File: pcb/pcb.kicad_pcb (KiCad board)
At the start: 2 copper layers, 33 parts, among them J1 USB_C_Receptacle_USB2.0_14P, J2 Conn_01x20, J3 Conn_01x20, J4 Conn_01x03, SW1 SW_Push, U1 RP2040, U2 NCP1117-3.3_SOT223, U3 W25Q128JVS, Y1 12 MHz

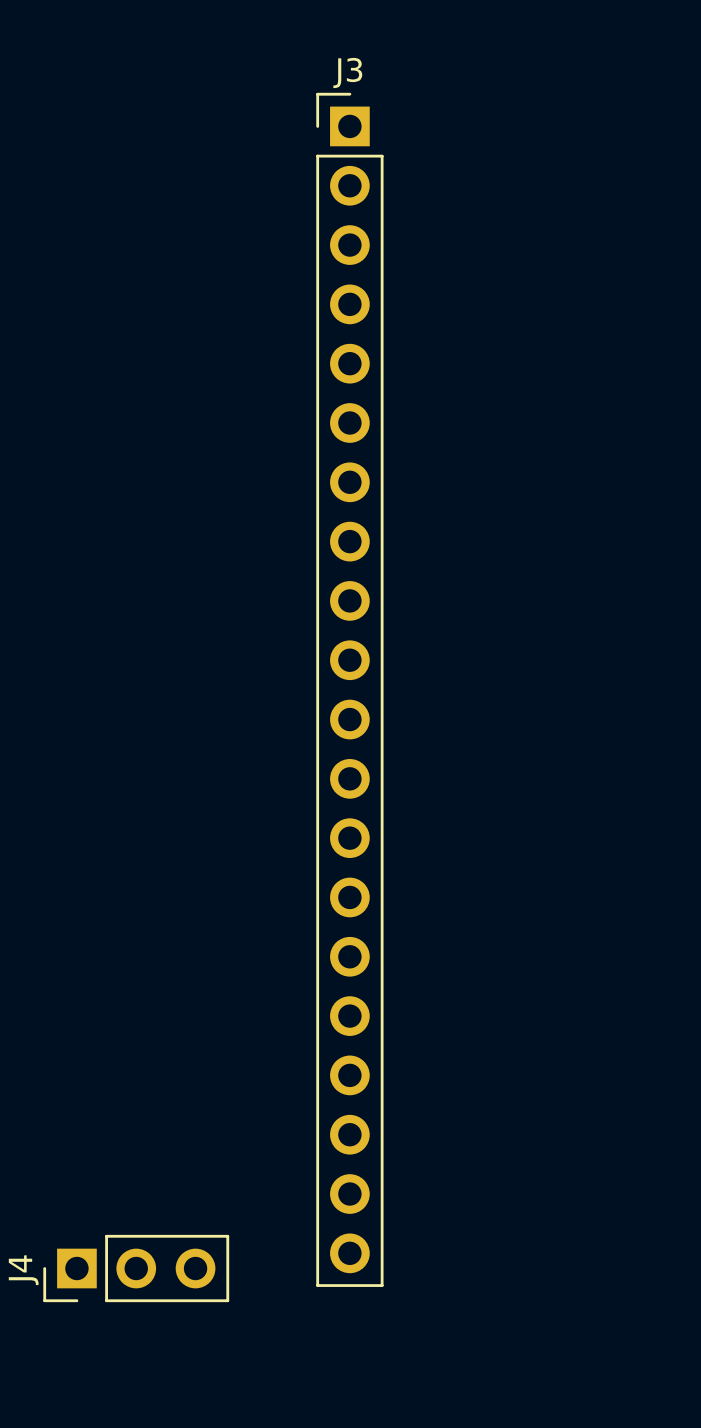
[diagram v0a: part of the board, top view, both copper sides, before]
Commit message: feat: added the neopixel status led
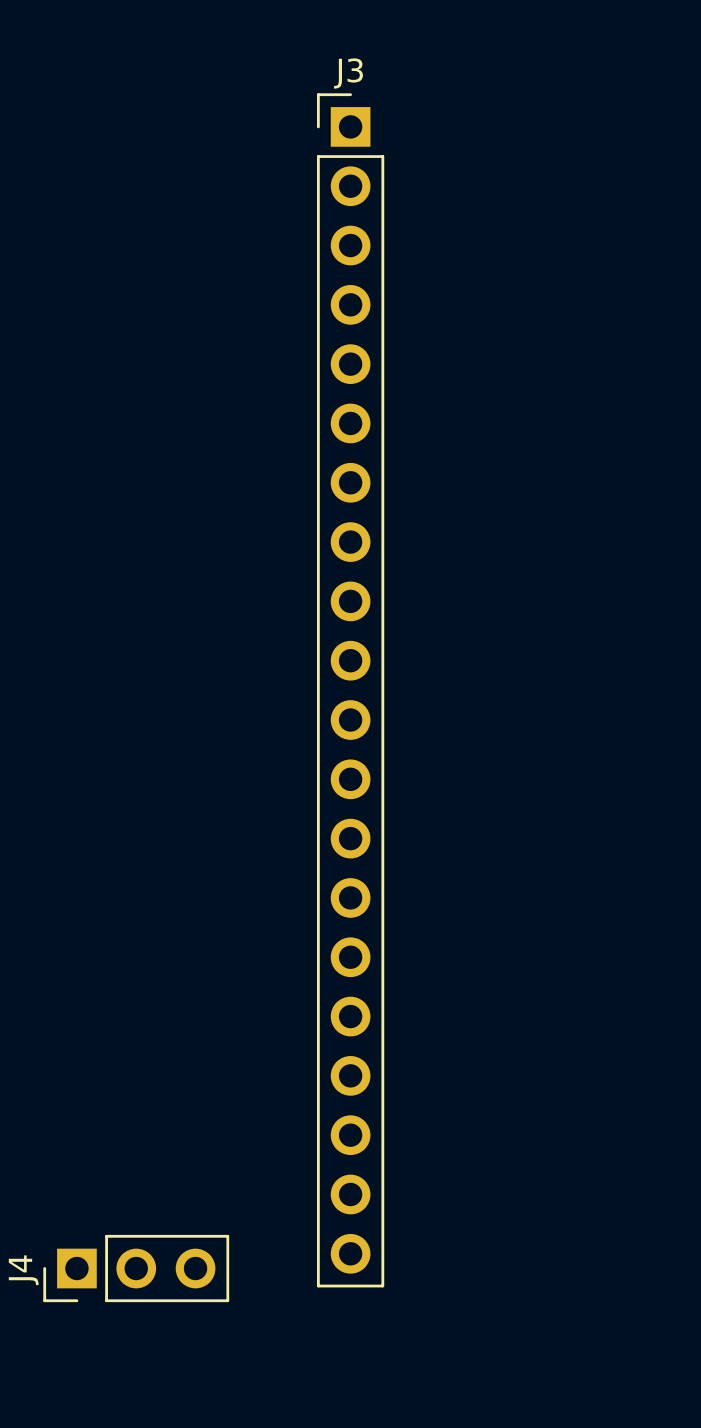
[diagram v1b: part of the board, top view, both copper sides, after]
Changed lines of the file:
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@@
 	(footprint "Connector_PinHeader_2.54mm:PinHeader_1x20_P2.54mm_Vertical"
 		(layer "F.Cu")
-		(at 133.35 61.94)
+		(at 133.38 61.96)
 		(descr "Through hole straight pin header, 1x20, 2.54mm pitch, single row")
 		(tags "Through hole pin header THT 1x20 2.54mm single row")
@@
 			)
 		)
+	)
+	(dimension
+		(type orthogonal)
+		(layer "F.Cu")
+		(pts
+			(xy 135.15 111.99) (xy 114.15 111.99)
+		)
+		(height 3.35)
+		(orientation 0)
+		(format
+			(prefix "")
+			(suffix "")
+			(units 3)
+			(units_format 0)
+			(precision 4)
+			(suppress_zeroes yes)
+		)
+		(style
+			(thickness 0.2)
+			(arrow_length 1.27)
+			(text_position_mode 0)
+			(arrow_direction outward)
+			(extension_height 0.58642)
+			(extension_offset 0.5)
+			(keep_text_aligned yes)
+		)
+		(gr_text "21"
+			(at 124.65 113.54 0)
+			(layer "F.Cu")
+			(effects
+				(font
+					(size 1.5 1.5)
+					(thickness 0.3)
+				)
+			)
+		)

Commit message: finished the schematic and added it to the pcb
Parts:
- added D2: APA102, LED_SMD:LED_RGB_5050-6, F.Cu at (201.1, 61.7)
- moved J1 18.5 mm to (184.9, 92.1)
- moved U1 15.4 mm to (186.9, 104.5)
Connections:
- J2 pad 11: GPIO8 -> unconnected-(J2-Pin_11-Pad11)
- J2 pad 12: GPIO9 -> unconnected-(J2-Pin_12-Pad12)

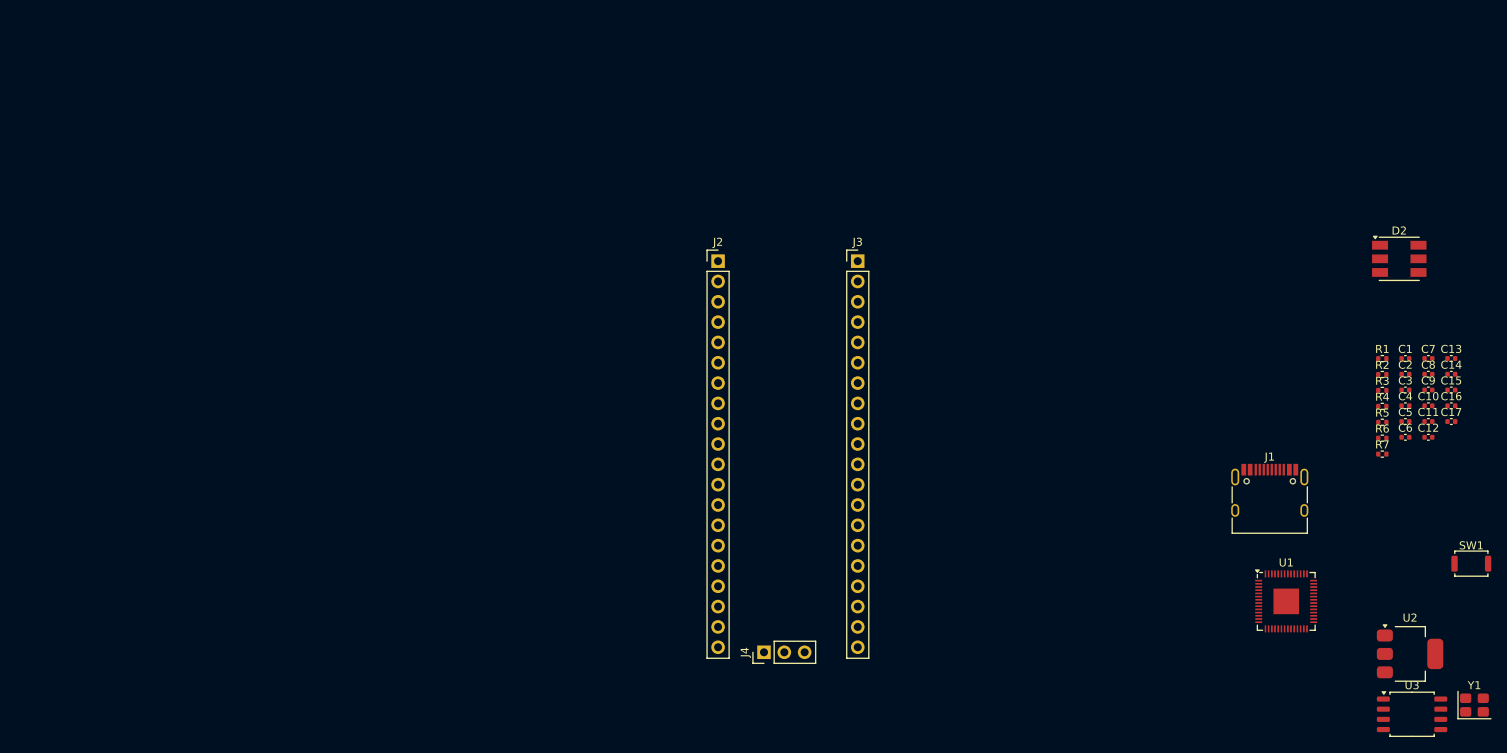
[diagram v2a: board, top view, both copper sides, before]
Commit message: updated the schematic with better formatting
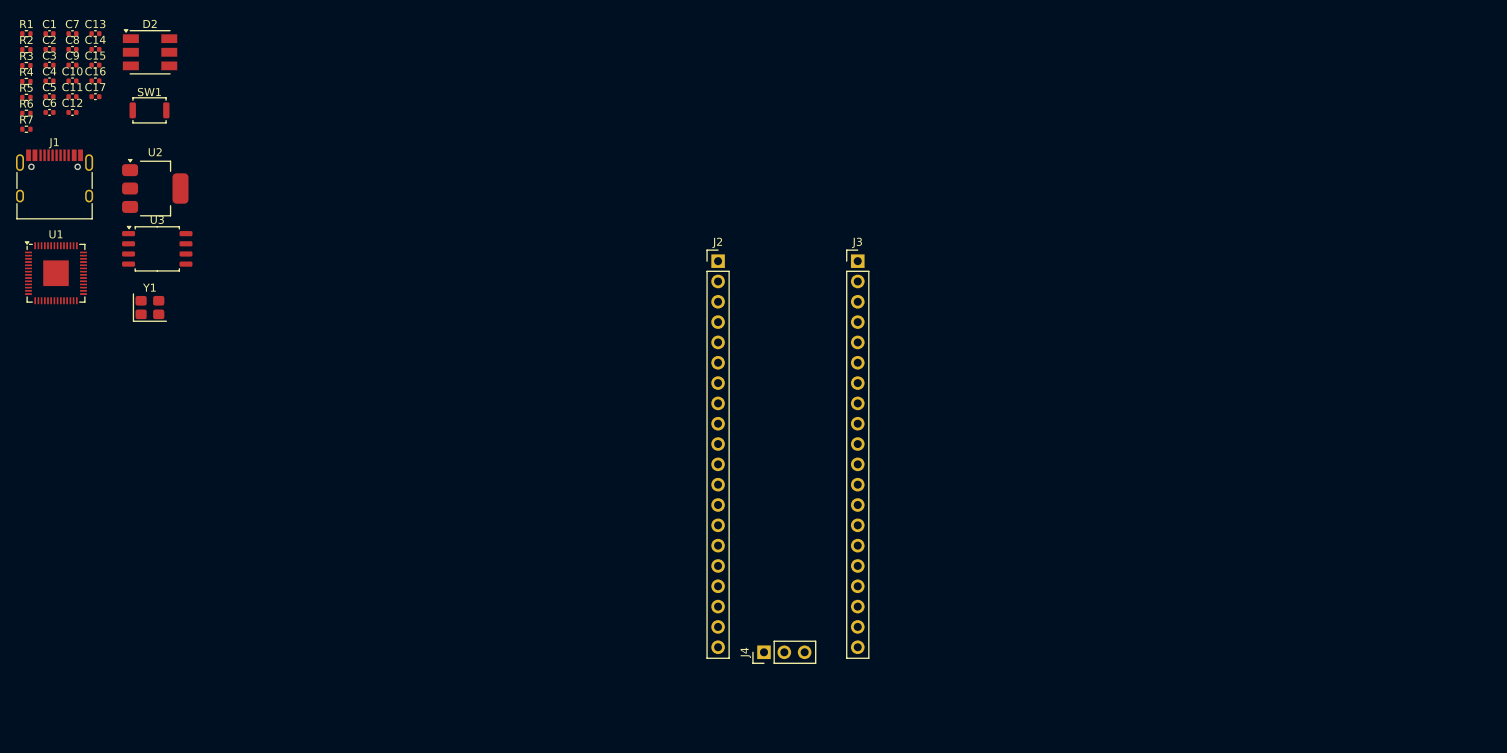
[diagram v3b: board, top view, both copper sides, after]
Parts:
- moved SW1 174.7 mm to (44.9, 43.1)
- moved C1 174.3 mm to (32.4, 33.5)
- moved C10 174.3 mm to (35.2, 39.4)
- moved C11 174.3 mm to (35.2, 41.4)
- moved C12 174.3 mm to (35.2, 43.4)
- moved C13 174.3 mm to (38.1, 33.5)
- moved C14 174.3 mm to (38.1, 35.5)
- moved C15 174.3 mm to (38.1, 37.5)
- moved C16 174.3 mm to (38.1, 39.4)
- moved C17 174.3 mm to (38.1, 41.4)
- moved C2 174.3 mm to (32.4, 35.5)
- moved C3 174.3 mm to (32.4, 37.5)
- moved C4 174.3 mm to (32.4, 39.4)
- moved C5 174.3 mm to (32.4, 41.4)
- moved C6 174.3 mm to (32.4, 43.4)
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
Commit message: feat: updated most of the pcb, still have some capacitors to wire
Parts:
- added C18: 0.1uF, Capacitor_SMD:C_0402_1005Metric, F.Cu at (131.5, 99.3)
- added R8: 100, Resistor_SMD:R_0402_1005Metric, F.Cu at (132.0, 94.5)
- added R9: 100, Resistor_SMD:R_0402_1005Metric, F.Cu at (132.0, 96.5)
- C1: value 0.1uF -> 1uF
- C9: value 1uF -> 0.1uF
- U2: value NCP1117-3.3_SOT223 -> MCP1700x-330xxTT; footprint Package_TO_SOT_SMD:SOT-223-3_TabPin2 -> Package_TO_SOT_SMD:SOT-23
- U3: value W25Q128JVS -> W25Q16JVZPIQ; footprint Package_SO:SOIC-8_5.3x5.3mm_P1.27mm -> Package_SON:Winbond_USON-8-1EP_3x2mm_P0.5mm_EP0.2x1.6mm
- moved C10 97.1 mm to (113.5, 96.8), turned to 90 degrees
- moved C7 96.3 mm to (120.8, 77.6), turned to 90 degrees
- moved C2 94.6 mm to (103.3, 98.0), turned to -90 degrees
- moved C6 94.2 mm to (119.8, 78.2), turned to -90 degrees
- moved C1 91.8 mm to (106.8, 87.2), turned to 45 degrees
- moved R5 91.6 mm to (101.7, 97.8)
- moved C9 90.7 mm to (106.9, 93.1)
- moved D2 90.3 mm to (101.4, 106.3)
- moved C8 89.1 mm to (106.7, 88.7)
- moved C16 89.0 mm to (103.3, 100.0), turned to 90 degrees
- moved R3 87.9 mm to (102.2, 86.8), turned to -90 degrees
- moved R4 87.7 mm to (103.3, 86.8), turned to -90 degrees
- moved C15 86.7 mm to (97.9, 100.2), turned to -90 degrees
- moved C5 86.2 mm to (105.3, 87.3), turned to 90 degrees
- moved C3 85.0 mm to (96.3, 93.4), turned to 180 degrees
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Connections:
- C17 pad 1: +3V3 -> GND
- C17 pad 2: GND -> +3V3
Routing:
- net +3V3: track 0.00 -> 67.8 mm, vias 0 -> 3
- net GPIO0: track 0.00 -> 26.8 mm, vias 0 -> 1
- net GPIO1: track 0.00 -> 25.0 mm, vias 0 -> 2
- net GPIO15: track 0.00 -> 23.5 mm
- net GPIO29_ADC3: track 0.00 -> 23.4 mm, vias 0 -> 1
- net SWCLK: track 0.00 -> 22.8 mm, vias 0 -> 1
- net GPIO16: track 0.00 -> 21.7 mm
- net SWD: track 0.00 -> 21.7 mm, vias 0 -> 1
- net GPIO14: track 0.00 -> 20.8 mm
- net GPIO2: track 0.00 -> 20.4 mm, vias 0 -> 2
- net GPIO28_ADC2: track 0.00 -> 20.1 mm
- net VBUS: track 0.00 -> 20.0 mm
- net USB_D-: track 0.00 -> 19.9 mm
- net GPIO17: track 0.00 -> 19.4 mm
- net QSPI_SS: track 0.00 -> 19.1 mm, vias 0 -> 2
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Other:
- board outline added: 21 x 51 mm

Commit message: holy shit massive update the pcb routing is done
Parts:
- moved R8 37.2 mm to (96.7, 106.3)
- moved R9 36.3 mm to (96.6, 104.8)
- moved C18 27.1 mm to (105.7, 107.6), turned to 90 degrees
- moved C7 19.3 mm to (102.3, 83.0), turned to 180 degrees
- moved C6 18.2 mm to (102.8, 84.4), turned to 90 degrees
- moved C10 9.01 mm to (104.5, 98.1), turned to -90 degrees
- moved J2 0.09 mm to (92.5, 66.2)
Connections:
- J2 pad 11: unconnected-(J2-Pin_11-Pad11) -> GPIO8
- J2 pad 12: unconnected-(J2-Pin_12-Pad12) -> GPIO9
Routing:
- net GND: track 9.28 -> 112.6 mm, vias 4 -> 41
- net +3V3: track 67.8 -> 99.7 mm, vias 3 -> 6
- net GPIO8: track 0.00 -> 26.6 mm, vias 0 -> 2
- net +1V1: track 5.54 -> 28.6 mm, vias 0 -> 2
- net GPIO9: track 0.00 -> 20.5 mm, vias 0 -> 2
- net XIN: track 1.71 -> 12.2 mm, vias 0 -> 2
- net XOUT: track 0.00 -> 2.58 mm
- net Net-(D2-DI): track 0.00 -> 1.96 mm
- net Net-(D2-CI): track 0.00 -> 1.84 mm
- net GPIO29_ADC3: track 23.4 -> 25.1 mm
- net USB_D+: track 18.6 -> 20.3 mm
- net USB_D-: track 19.9 -> 20.8 mm
- net GPIO1: track 25.0 -> 24.9 mm, vias 2 -> 1
- added copper zone on B.Cu, net GND
- added copper zone on F.Cu, net GND
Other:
- board size 21 x 51 mm -> 21 x 51.1 mm

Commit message: better routing completed
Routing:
- net GND: track 112.6 -> 112.8 mm, vias 41 -> 82

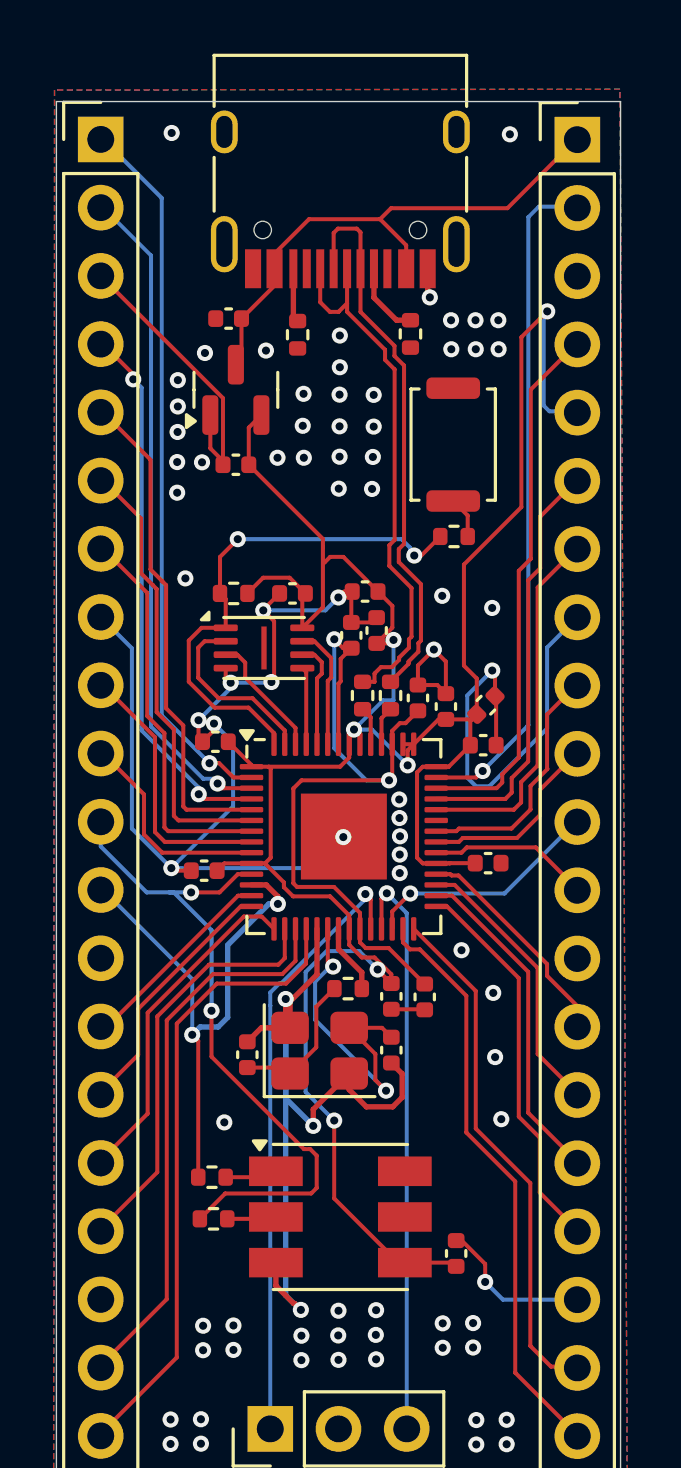
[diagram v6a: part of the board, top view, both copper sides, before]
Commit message: added some more vias and lined them up
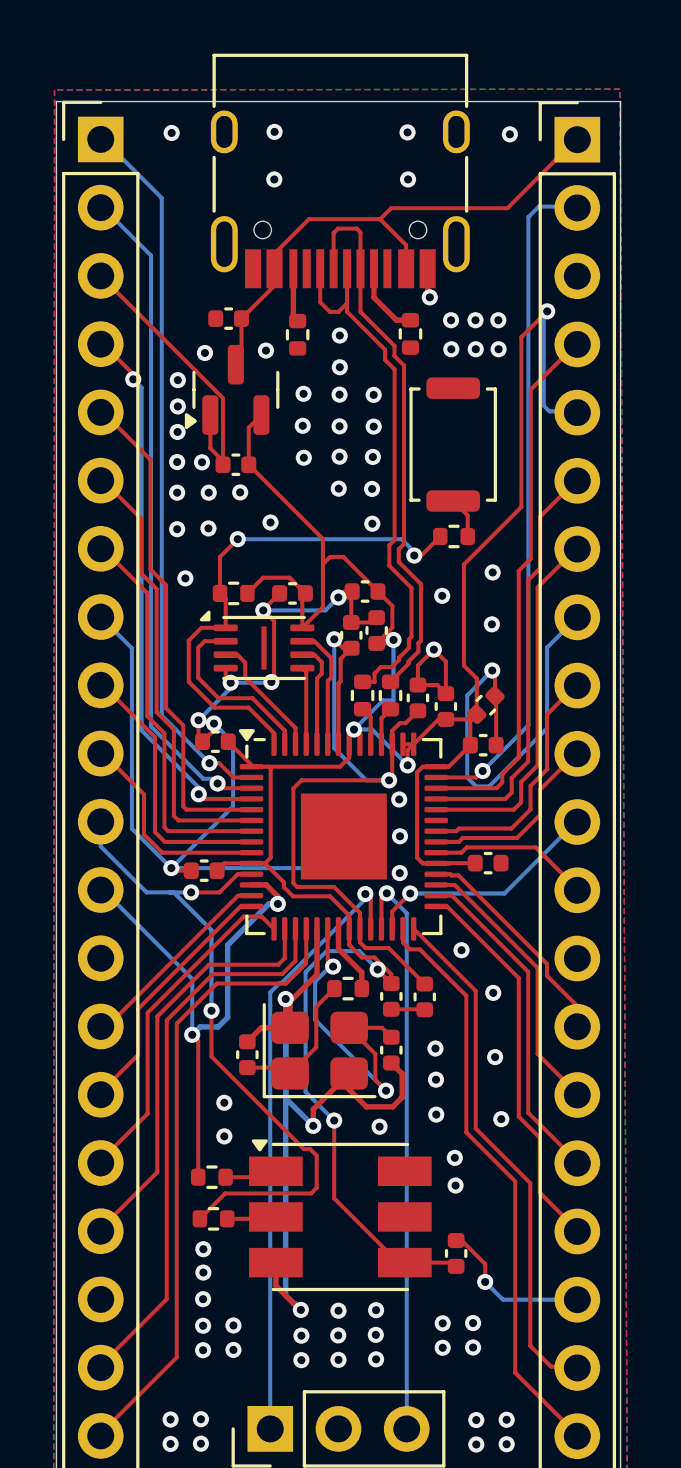
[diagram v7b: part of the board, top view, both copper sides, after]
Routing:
- net GND: vias 82 -> 99
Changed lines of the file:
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@@
 	)
 	(via
-		(at 103.61 92.77)
-		(size 0.6)
-		(drill 0.3)
-		(layers "F.Cu" "B.Cu")
-		(net 1)
-	)
-	(via
 		(at 105.19 83.14)
 		(size 0.6)
@@
 	)
 	(via
-		(at 101.51 92.12)
+		(at 95.108172 93.274999)
 		(size 0.6)
 		(drill 0.3)
@@
 	)
 	(via
-		(at 95.108172 93.274999)
+		(at 107.28 72.88)
 		(size 0.6)
 		(drill 0.3)
 		(layers "F.Cu" "B.Cu")
+		(free yes)
 		(net 1)
 	)
 	(via
-		(at 107.28 72.88)
+		(at 98.8 80.41)
 		(size 0.6)
 		(drill 0.3)
@@
 	)
 	(via
+		(at 96.29 109.32)
+		(size 0.6)
+		(drill 0.3)
+		(layers "F.Cu" "B.Cu")
+		(free yes)
+		(net 1)
+	)
+	(via
 		(at 96.12 87.77)
 		(size 0.6)
@@
 	)
 	(via
+		(at 98.94 67.64)
+		(size 0.6)
+		(drill 0.3)
+		(layers "F.Cu" "B.Cu")
+		(free yes)
+		(net 1)
+	)
+	(via
 		(at 99.95 110.68)
 		(size 0.6)
@@
 	)
 	(via
+		(at 102.86 102.9)
+		(size 0.6)
+		(drill 0.3)
+		(layers "F.Cu" "B.Cu")
+		(free yes)
+		(net 1)
+	)
+	(via
+		(at 104.94 99.99)
+		(size 0.6)
+		(drill 0.3)
+		(layers "F.Cu" "B.Cu")
+		(free yes)
+		(net 1)
+	)
+	(via
 		(at 96.29 110.31)
 		(size 0.6)
@@
 	)
 	(via
+		(at 102.59 80.455)
+		(size 0.6)
+		(drill 0.3)
+		(layers "F.Cu" "B.Cu")
+		(free yes)
+		(net 1)
+	)
+	(via
 		(at 99.365 98.14726)
 		(size 0.6)
@@
 	)
 	(via
+		(at 103.92 67.64)
+		(size 0.6)
+		(drill 0.3)
+		(layers "F.Cu" "B.Cu")
+		(free yes)
+		(net 1)
+	)
+	(via
+		(at 97.67 79.29)
+		(size 0.6)
+		(drill 0.3)
+		(layers "F.Cu" "B.Cu")
+		(free yes)
+		(net 1)
+	)
+	(via
 		(at 98.53079 83.680908)
 		(size 0.6)
@@
 	)
 	(via
+		(at 104.97 102.45)
+		(size 0.6)
+		(drill 0.3)
+		(layers "F.Cu" "B.Cu")
+		(free yes)
+		(net 1)
+	)
+	(via
 		(at 106.34 110.21)
 		(size 0.6)
@@
 	)
 	(via
+		(at 103.9 65.89)
+		(size 0.6)
+		(drill 0.3)
+		(layers "F.Cu" "B.Cu")
+		(free yes)
+		(net 1)
+	)
+	(via
 		(at 106.46 114.73)
 		(size 0.6)
@@
 	)
 	(via
+		(at 104.96 101.15)
+		(size 0.6)
+		(drill 0.3)
+		(layers "F.Cu" "B.Cu")
+		(free yes)
+		(net 1)
+	)
+	(via
 		(at 95.08 114.71)
 		(size 0.6)
@@
 	)
 	(via
-		(at 107.05 83.59)
+		(at 107.04 84.2)
 		(size 0.6)
 		(drill 0.3)
@@
 	)
 	(via
+		(at 96.3 108.33)
+		(size 0.6)
+		(drill 0.3)
+		(layers "F.Cu" "B.Cu")
+		(free yes)
+		(net 1)
+	)
+	(via
 		(at 102.58 79.16)
 		(size 0.6)
@@
 	)
 	(via
-		(at 95.12 65.91)
+		(at 98.95 65.87)
 		(size 0.6)
 		(drill 0.3)
@@
 	)
 	(via
-		(at 103.6 91.41)
+		(at 95.12 65.91)
 		(size 0.6)
 		(drill 0.3)
 		(layers "F.Cu" "B.Cu")
+		(free yes)
 		(net 1)
 	)
@@
 	)
 	(via
+		(at 96.49 80.63)
+		(size 0.6)
+		(drill 0.3)
+		(layers "F.Cu" "B.Cu")
+		(free yes)
+		(net 1)
+	)
+	(via
 		(at 101.325 83.2)
 		(size 0.6)
@@
 	)
 	(via
-		(at 97.08 102.74)
+		(at 97.08 102.01)
 		(size 0.6)
 		(drill 0.3)
@@
 	)
 	(via
-		(at 99.06 78)
+		(at 97.08 103.26)
 		(size 0.6)
 		(drill 0.3)
@@
 	)
 	(via
+		(at 105.69 105.09)
+		(size 0.6)
+		(drill 0.3)
+		(layers "F.Cu" "B.Cu")
+		(free yes)
+		(net 1)
+	)
+	(via
 		(at 95.35 76.09)
 		(size 0.6)
@@
 	)
 	(via
+		(at 96.5 79.3)
+		(size 0.6)
+		(drill 0.3)
+		(layers "F.Cu" "B.Cu")
+		(free yes)
+		(net 1)
+	)
+	(via
 		(at 95.34 77.04)
 		(size 0.6)
@@
 	)
 	(via
+		(at 107.07 82.27)
+		(size 0.6)
+		(drill 0.3)
+		(layers "F.Cu" "B.Cu")
+		(free yes)
+		(net 1)
+	)
+	(via
+		(at 95.325 80.66)
+		(size 0.6)
+		(drill 0.3)
+		(layers "F.Cu" "B.Cu")
+		(free yes)
+		(net 1)
+	)
+	(via
 		(at 101.37 76.83)
 		(size 0.6)
@@
 	)
 	(via
+		(at 96.3 107.46)
+		(size 0.6)
+		(drill 0.3)
+		(layers "F.Cu" "B.Cu")
+		(free yes)
+		(net 1)
+	)
+	(via
 		(at 96.694923 87.89293)
 		(size 0.6)
@@
 	)
 	(via
+		(at 105.66 104.06)
+		(size 0.6)
+		(drill 0.3)
+		(layers "F.Cu" "B.Cu")
+		(free yes)
+		(net 1)
+	)
+	(via
 		(at 96.36 74.1)
 		(size 0.6)
@@
 		(polygon
 			(pts
-				(xy 90.760157 64.310128) (xy 90.73 116.07) (xy 112.08 116.07) (xy 111.81 64.28) (xy 90.760157 64.310128)
+				(xy 90.760157 64.310128) (xy 90.73 116.07) (xy 112.08 116.07) (xy 111.81 64.28)
 			)
 		)
